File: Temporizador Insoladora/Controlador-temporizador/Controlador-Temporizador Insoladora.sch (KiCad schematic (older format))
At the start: 72 parts, among them P1 ICSP, P2 CONN_01X03, P3 CARGA, P4 TRANSF, P5 VAC, P7 CONN_02X08, Q1 BC548, Q2 BC548, Q3 BC548, Q4 BC548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

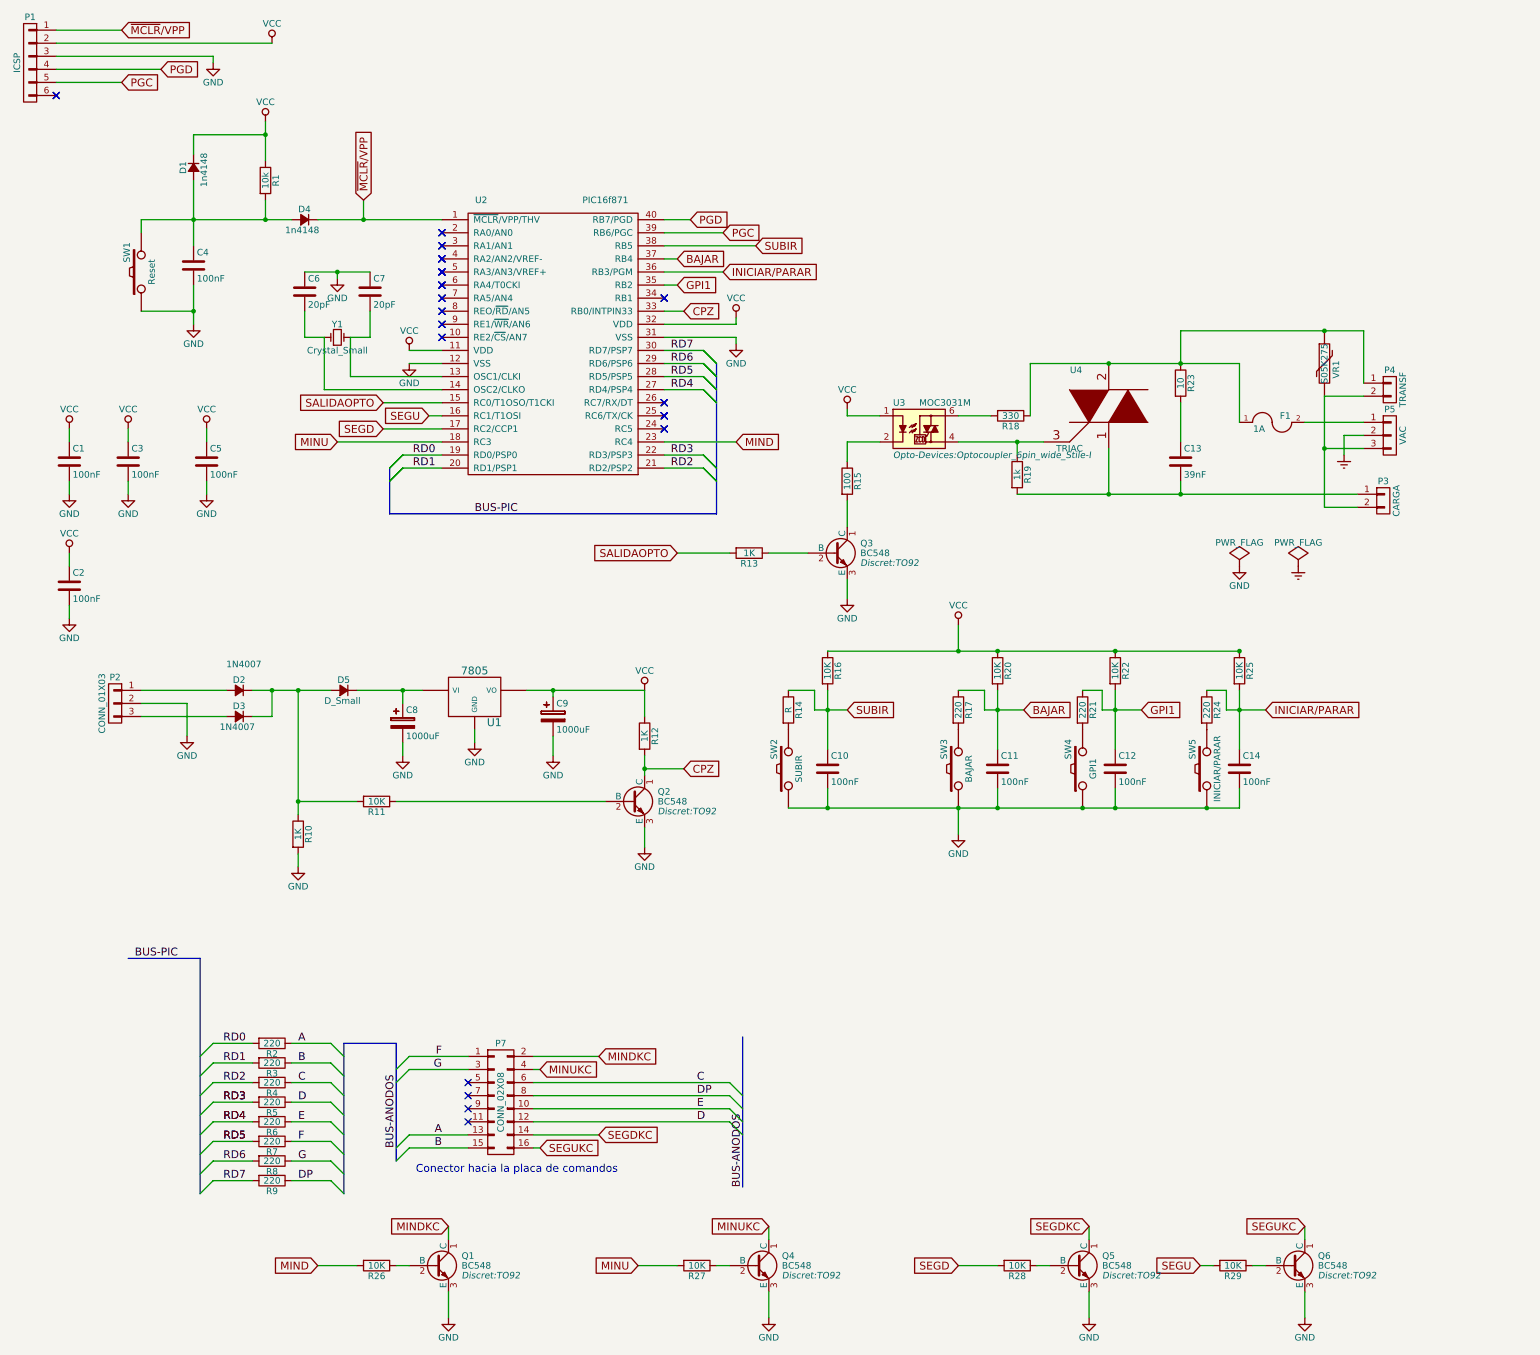
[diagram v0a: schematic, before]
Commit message: Comienzo a diseñar el controlador
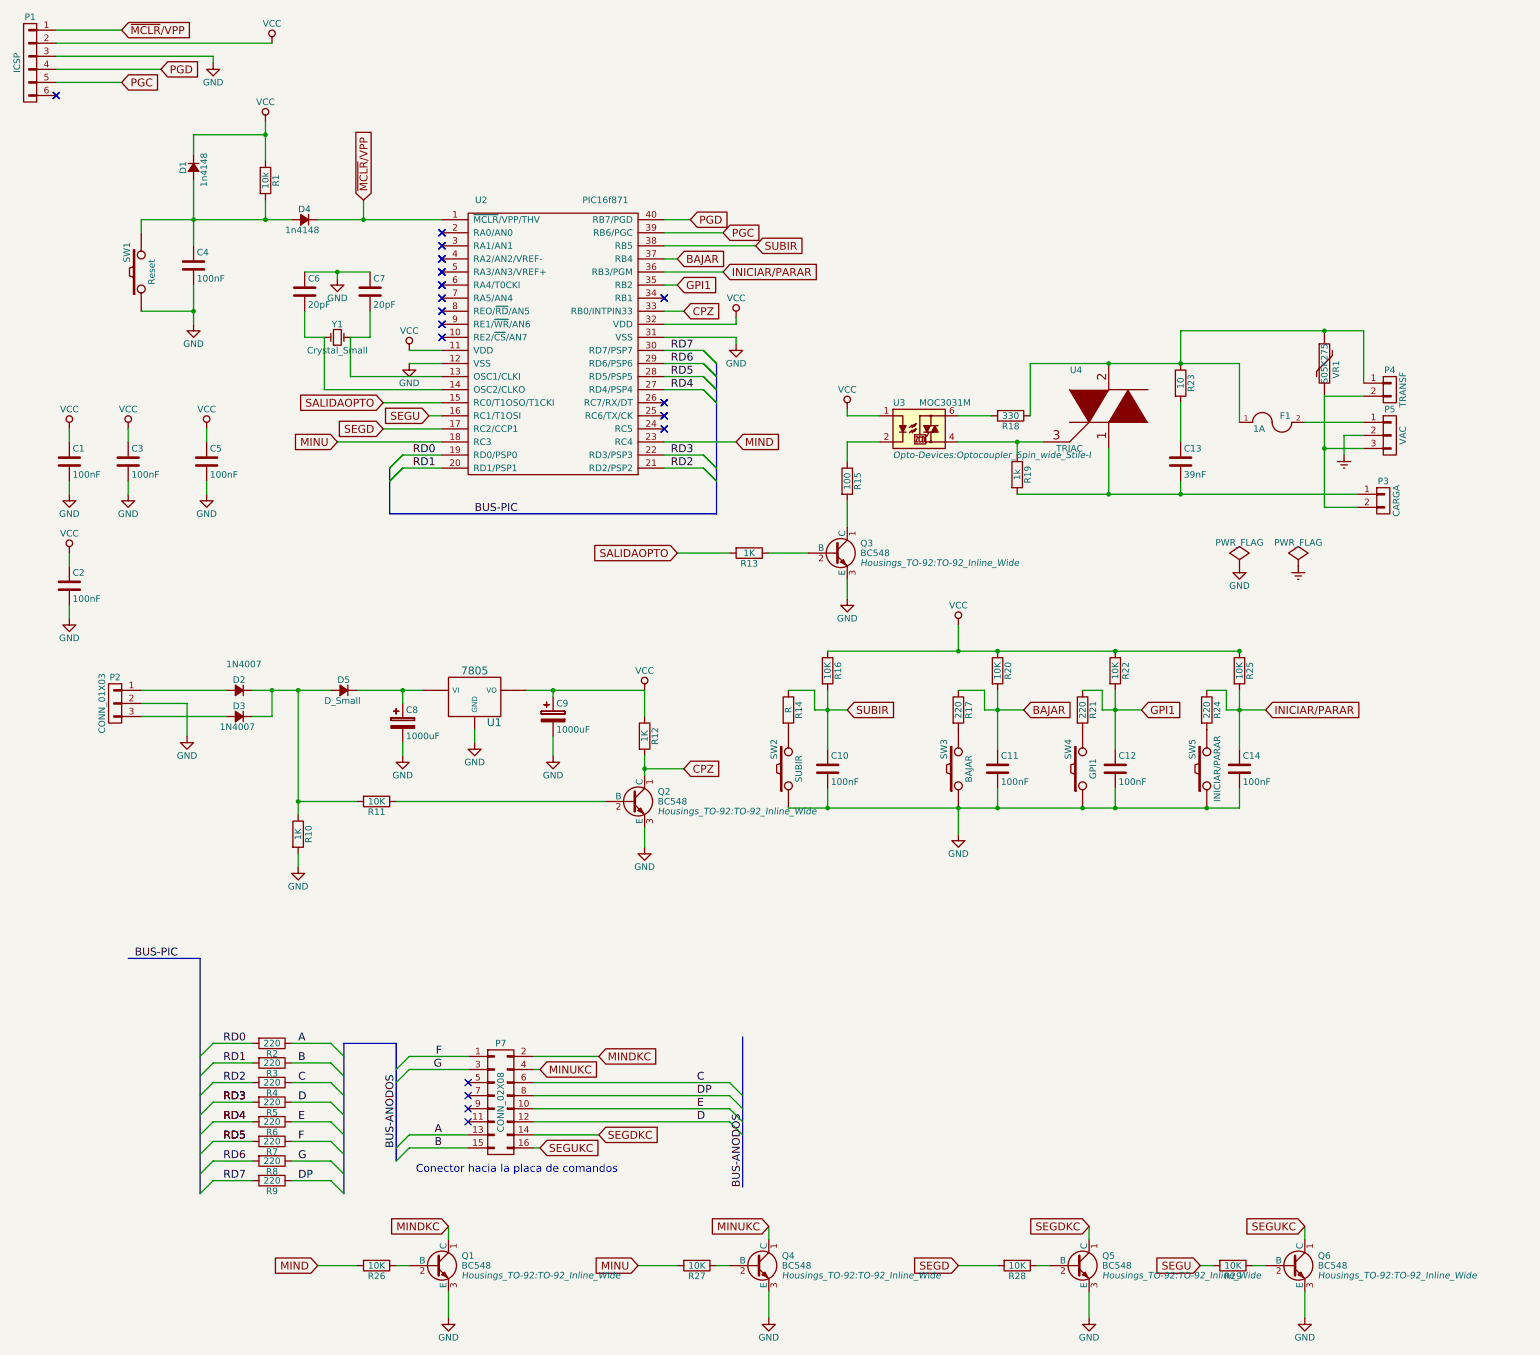
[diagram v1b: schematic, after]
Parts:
- P7: footprint Connect:VASCH8x2 -> Socket_Strips:Socket_Strip_Straight_2x08
- Q1, Q2, Q3, Q4, Q5, Q6: footprint Discret:TO92 -> Housings_TO-92:TO-92_Inline_Wide
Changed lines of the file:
@@
 F 0 "Q2" H 5600 6575 50  0000 L CNN
 F 1 "BC548" H 5600 6500 50  0000 L CNN
-F 2 "Discret:TO92" H 5600 6425 50  0000 L CIN
+F 2 "Housings_TO-92:TO-92_Inline_Wide" H 5600 6425 50  0000 L CIN
 F 3 "" H 5400 6500 50  0000 L CNN
 	1    5400 6500
@@
 F 0 "Q3" H 7150 4675 50  0000 L CNN
 F 1 "BC548" H 7150 4600 50  0000 L CNN
-F 2 "Discret:TO92" H 7150 4525 50  0000 L CIN
+F 2 "Housings_TO-92:TO-92_Inline_Wide" H 7150 4525 50  0000 L CIN
 F 3 "" H 6950 4600 50  0000 L CNN
 	1    6950 4600
@@
 F 0 "Q1" H 4100 10125 50  0000 L CNN
 F 1 "BC548" H 4100 10050 50  0000 L CNN
-F 2 "Discret:TO92" H 4100 9975 50  0000 L CIN
+F 2 "Housings_TO-92:TO-92_Inline_Wide" H 4100 9975 50  0000 L CIN
 F 3 "" H 3900 10050 50  0000 L CNN
 	1    3900 10050
@@
 F 0 "Q4" H 6550 10125 50  0000 L CNN
 F 1 "BC548" H 6550 10050 50  0000 L CNN
-F 2 "Discret:TO92" H 6550 9975 50  0000 L CIN
+F 2 "Housings_TO-92:TO-92_Inline_Wide" H 6550 9975 50  0000 L CIN
 F 3 "" H 6350 10050 50  0000 L CNN
 	1    6350 10050
@@
 F 0 "Q5" H 9000 10125 50  0000 L CNN
 F 1 "BC548" H 9000 10050 50  0000 L CNN
-F 2 "Discret:TO92" H 9000 9975 50  0000 L CIN
+F 2 "Housings_TO-92:TO-92_Inline_Wide" H 9000 9975 50  0000 L CIN
 F 3 "" H 8800 10050 50  0000 L CNN
 	1    8800 10050
@@
 F 0 "Q6" H 10650 10125 50  0000 L CNN
 F 1 "BC548" H 10650 10050 50  0000 L CNN
-F 2 "Discret:TO92" H 10650 9975 50  0000 L CIN
+F 2 "Housings_TO-92:TO-92_Inline_Wide" H 10650 9975 50  0000 L CIN
 F 3 "" H 10450 10050 50  0000 L CNN
 	1    10450 10050
@@
 F 0 "P7" H 4400 9250 50  0000 C CNN
 F 1 "CONN_02X08" V 4400 8800 50  0000 C CNN
-F 2 "Connect:VASCH8x2" H 4400 7600 60  0001 C CNN
+F 2 "Socket_Strips:Socket_Strip_Straight_2x08" H 4400 7600 60  0001 C CNN
 F 3 "" H 4400 7600 60  0000 C CNN
 	1    4400 8800

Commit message: Sigo ruteando pcb controlador insoladora
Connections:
- net MINDKC: now also Q3.1 (C); no longer Q1.1 (C)
- net at R15.2: now also Q1.1 (C); no longer Q3.1 (C)
- net at Q3.2 (B): now also R26.1; no longer R13.1
- net at Q1.2 (B): now also R13.1; no longer R26.1
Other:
- moved on the sheet: Q1, Q3
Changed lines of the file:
@@
 L BC548 Q3
 U 1 1 552AB741
-P 6950 4600
-F 0 "Q3" H 7150 4675 50  0000 L CNN
-F 1 "BC548" H 7150 4600 50  0000 L CNN
-F 2 "Housings_TO-92:TO-92_Inline_Wide" H 7150 4525 50  0000 L CIN
-F 3 "" H 6950 4600 50  0000 L CNN
-	1    6950 4600
+P 3900 10050
+F 0 "Q3" H 4100 10125 50  0000 L CNN
+F 1 "BC548" H 4100 10050 50  0000 L CNN
+F 2 "Housings_TO-92:TO-92_Inline_Wide" H 4100 9975 50  0000 L CIN
+F 3 "" H 3900 10050 50  0000 L CNN
+	1    3900 10050
 	1    0    0    -1
 $EndComp
@@
 L BC548 Q1
 U 1 1 552AC2A5
-P 3900 10050
-F 0 "Q1" H 4100 10125 50  0000 L CNN
-F 1 "BC548" H 4100 10050 50  0000 L CNN
-F 2 "Housings_TO-92:TO-92_Inline_Wide" H 4100 9975 50  0000 L CIN
-F 3 "" H 3900 10050 50  0000 L CNN
-	1    3900 10050
-	1    0    0    -1
-$EndComp
+P 6950 4600
+F 0 "Q1" H 7150 4675 50  0000 L CNN
+F 1 "BC548" H 7150 4600 50  0000 L CNN
+F 2 "Housings_TO-92:TO-92_Inline_Wide" H 7150 4525 50  0000 L CIN
+F 3 "" H 6950 4600 50  0000 L CNN
+	1    6950 4600
+	1    0    0    -1
+$EndComp

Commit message: Sigo ruteando pcb controlador insoladora
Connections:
- net MIND: now also U2.18 (RC3); no longer U2.23 (RC4)
- net MINU: now also U2.17 (RC2/CCP1); no longer U2.18 (RC3)
- net SALIDAOPTO: now also U2.23 (RC4); no longer U2.15 (RC0/T1OSO/T1CKI)
- net SEGD: now also U2.16 (RC1/T1OSI); no longer U2.17 (RC2/CCP1)
- net SEGU: now also U2.15 (RC0/T1OSO/T1CKI); no longer U2.16 (RC1/T1OSI)
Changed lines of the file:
@@
 Wire Wire Line
 	6150 4600 5750 4600
-Wire Wire Line
-	3500 3450 3950 3450
 $Comp
 L GND #PWR020
@@
 	3000 10050 3300 10050
 Wire Wire Line
-	3850 3550 3950 3550
-Wire Wire Line
-	3500 3650 3950 3650
-Wire Wire Line
-	3150 3750 3950 3750
-Wire Wire Line
-	6200 3750 5650 3750
+	3400 3550 3950 3550
 $Comp
 L BC548 Q4
@@
 Text GLabel 3000 10050 0    60   Input ~ 0
 MIND
-Text GLabel 3850 3550 0    60   Input ~ 0
+Text GLabel 3800 3450 0    60   Input ~ 0
 SEGU
-Text GLabel 3500 3650 0    60   Input ~ 0
+Text GLabel 3400 3550 0    60   Input ~ 0
 SEGD
-Text GLabel 3150 3750 0    60   Input ~ 0
+Text GLabel 3050 3650 0    60   Input ~ 0
 MINU
-Text GLabel 6200 3750 2    60   Input ~ 0
+Text GLabel 3350 3750 0    60   Input ~ 0
 MIND
 Text GLabel 5450 10050 0    60   Input ~ 0
@@
 Text GLabel 5750 4600 0    60   Input ~ 0
 SALIDAOPTO
-Text GLabel 3500 3450 0    60   Input ~ 0
+Text GLabel 6250 3750 2    60   Input ~ 0
 SALIDAOPTO
 Text GLabel 3350 1900 1    60   Input ~ 0
@@
 Text Label 6250 9450 1    60   ~ 0
 BUS-ANODOS
+Wire Wire Line
+	6250 3750 5650 3750
+Wire Wire Line
+	3050 3650 3950 3650
+Wire Wire Line
+	3800 3450 3950 3450
+Wire Wire Line
+	3350 3750 3950 3750
 $EndSCHEMATC

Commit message: Acomodando el controlador
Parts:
- P2: value CONN_01X03 -> VAC12V
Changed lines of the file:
@@
 P 1450 5750
 F 0 "P2" H 1450 5950 50  0000 C CNN
-F 1 "CONN_01X03" V 1550 5750 50  0000 C CNN
+F 1 "VAC12V" V 1550 5750 50  0000 C CNN
 F 2 "Connect:bornier3" H 1450 5750 60  0001 C CNN
 F 3 "" H 1450 5750 60  0000 C CNN
